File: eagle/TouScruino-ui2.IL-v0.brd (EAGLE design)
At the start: 53.3 x 57.1 mm, 7 parts

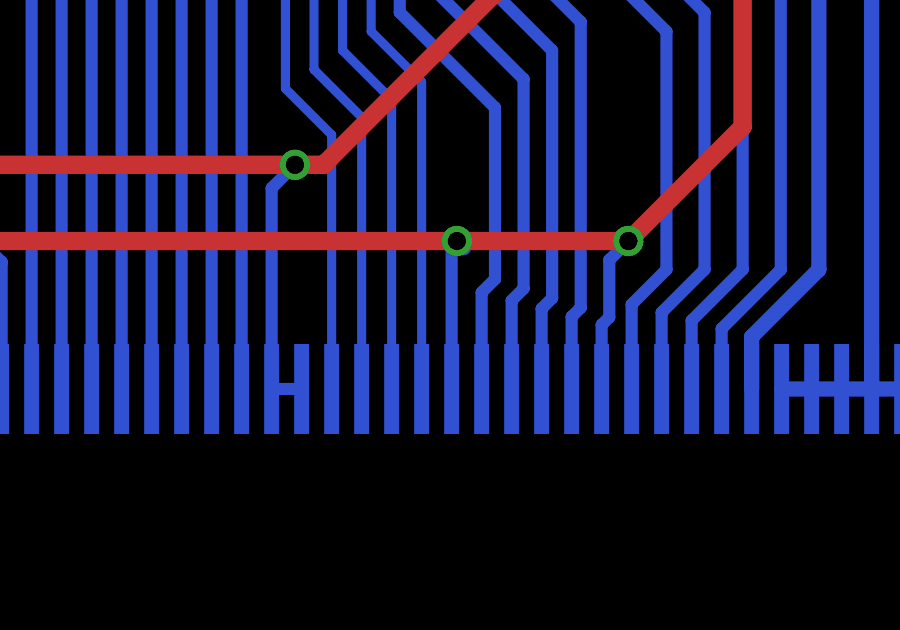
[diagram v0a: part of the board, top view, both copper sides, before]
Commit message: 
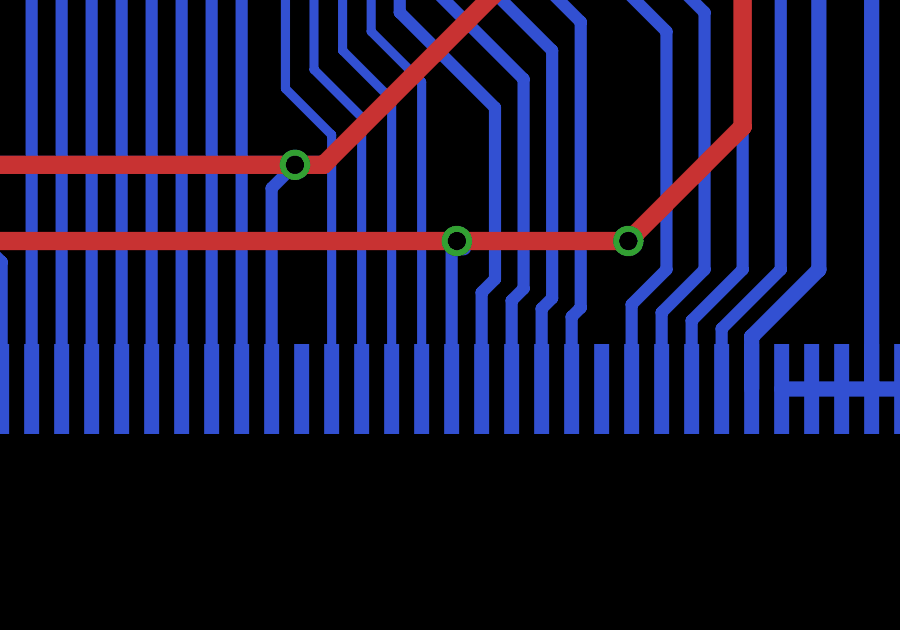
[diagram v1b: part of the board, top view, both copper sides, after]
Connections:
- net GND: no longer CN1.21
- net VCC: no longer CN1.11
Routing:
- net VCC: track 107.7 -> 102.4 mm
- net GND: track 112.2 -> 111.2 mm
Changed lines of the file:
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@@
 <setting verticaltext="up"/>
 </settings>
-<grid distance="12.5" unitdist="mil" unit="mm" style="lines" multiple="8" display="yes" altdistance="6.25" altunitdist="mil" altunit="mil"/>
+<grid distance="12.5" unitdist="mil" unit="mil" style="lines" multiple="8" display="yes" altdistance="6.25" altunitdist="mil" altunit="mil"/>
 <layers>
 <layer number="1" name="Top" color="4" fill="1" visible="yes" active="yes"/>
@@
 <layer number="220" name="220bmp" color="21" fill="1" visible="no" active="no"/>
 <layer number="221" name="221bmp" color="22" fill="1" visible="no" active="no"/>
+<layer number="222" name="222bmp" color="23" fill="1" visible="no" active="no"/>
 <layer number="223" name="223bmp" color="24" fill="1" visible="no" active="no"/>
 <layer number="224" name="224bmp" color="25" fill="1" visible="no" active="no"/>
@@
 <via x="24.4475" y="16.51" extent="1-16" drill="0.6096"/>
 <contactref element="CN1" pad="34"/>
-<contactref element="CN1" pad="21"/>
 <contactref element="CN1" pad="34"/>
 <contactref element="CN1" pad="5"/>
@@
 <wire x1="23.67" y1="9.0375" x2="23.67" y2="15.7325" width="0.4064" layer="16"/>
 <wire x1="23.67" y1="15.7325" x2="24.4475" y2="16.51" width="0.4064" layer="16"/>
-<wire x1="23.67" y1="9.0375" x2="24.67" y2="9.0375" width="0.4064" layer="16"/>
 <wire x1="43.67" y1="9.0375" x2="43.67" y2="28.72" width="0.508" layer="16"/>
 <wire x1="40.67" y1="9.0375" x2="41.67" y2="9.0375" width="0.508" layer="16"/>
@@
 <wire x1="41.91" y1="13.0175" x2="41.91" y2="25.4" width="0.508" layer="16"/>
 <wire x1="41.91" y1="25.4" x2="39.37" y2="27.94" width="0.508" layer="16"/>
-<wire x1="34.925" y1="13.335" x2="35.56" y2="13.97" width="0.4064" layer="16"/>
 <via x="35.56" y="13.97" extent="1-16" drill="0.6096"/>
 <contactref element="CN1" pad="16"/>
-<contactref element="CN1" pad="11"/>
 <contactref element="CN1" pad="32"/>
 <contactref element="CN1" pad="33"/>
@@
 <wire x1="29.67" y1="9.0375" x2="29.67" y2="13.795" width="0.4064" layer="16"/>
 <wire x1="29.67" y1="13.795" x2="29.845" y2="13.97" width="0.4064" layer="16"/>
-<wire x1="34.67" y1="9.0375" x2="34.67" y2="11.175" width="0.4064" layer="16"/>
-<wire x1="34.67" y1="11.175" x2="34.925" y2="11.43" width="0.4064" layer="16"/>
-<wire x1="34.925" y1="11.43" x2="34.925" y2="13.335" width="0.4064" layer="16"/>
 <wire x1="39.67" y1="9.0375" x2="39.67" y2="10.7775" width="0.508" layer="16"/>
 <wire x1="39.67" y1="10.7775" x2="41.91" y2="13.0175" width="0.508" layer="16"/>
